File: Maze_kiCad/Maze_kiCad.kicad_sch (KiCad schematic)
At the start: 9 parts, among them U1 ESP32-S2-DevKitC-1, U2 TSSP58038, U3 TSSP58038, U4 TSSP58038, U5 TSSP58038, U6 TSSP58038, U7 TSSP58038, U8 GY-521

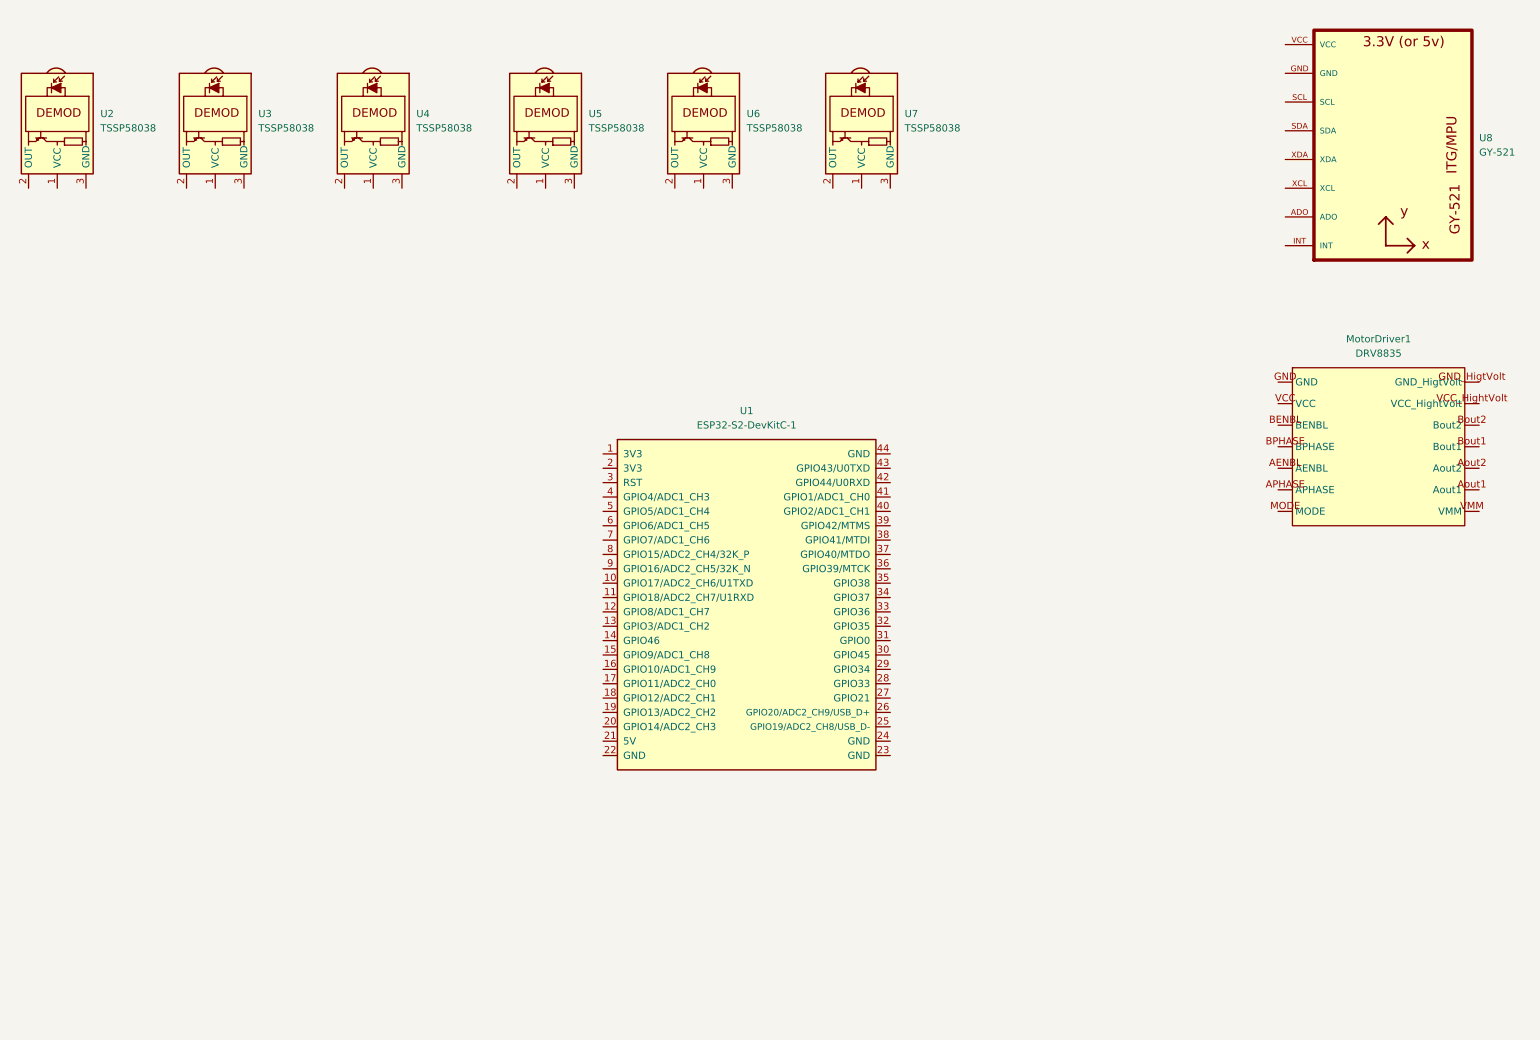
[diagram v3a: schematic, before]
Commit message: add ultra sonic symbol and footprint
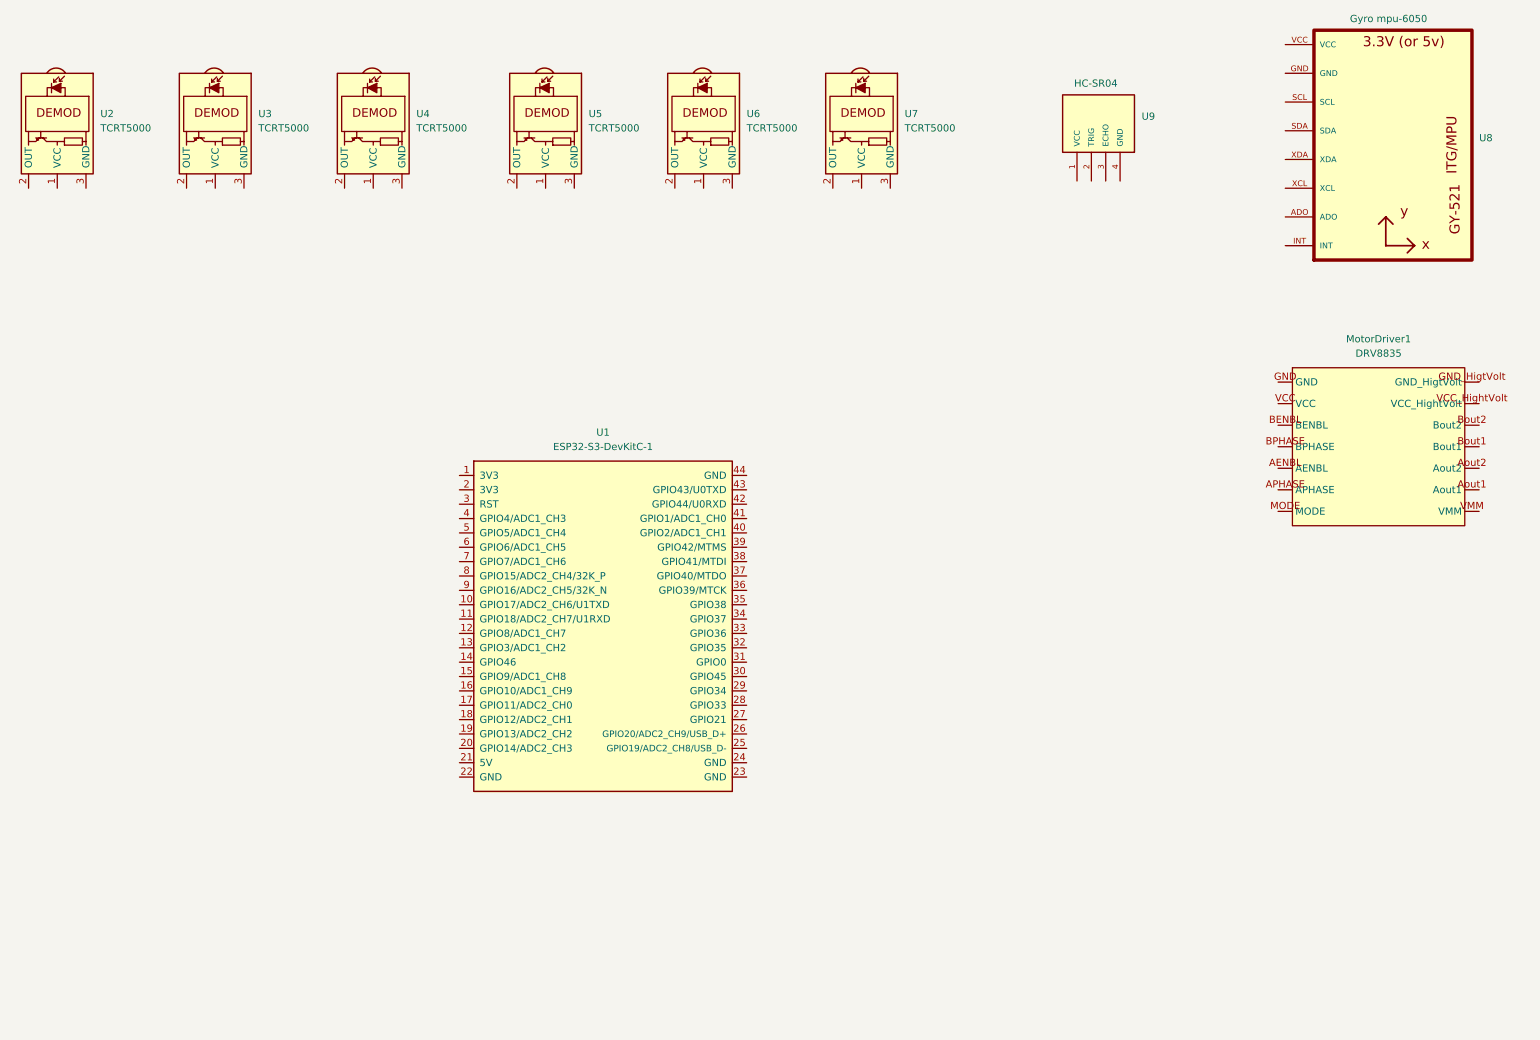
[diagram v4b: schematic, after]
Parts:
- added U9: HC-SR04, ultrasonic:XCVR_HC-SR04, symbol ultrasonic:HC-SR04
- U1: value ESP32-S2-DevKitC-1 -> ESP32-S3-DevKitC-1
- U2, U3, U4, U5, U6, U7: value TSSP58038 -> TCRT5000
- U8: value GY-521 -> Gyro mpu-6050
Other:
- moved on the sheet: U1
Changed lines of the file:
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@@
 			)
 		)
-		(property "Value" "TSSP58038"
+		(property "Value" "TCRT5000"
 			(at 144.78 35.0949 90)
 			(effects
@@
 			)
 		)
-		(property "Value" "TSSP58038"
+		(property "Value" "TCRT5000"
 			(at 116.84 35.0949 90)
 			(effects
@@
 			)
 		)
-		(property "Value" "TSSP58038"
+		(property "Value" "TCRT5000"
 			(at 30.48 35.0949 90)
 			(effects
@@
 			)
 		)
-		(property "Value" "TSSP58038"
+		(property "Value" "TCRT5000"
 			(at 58.42 35.0949 90)
 			(effects
@@
 			)
 		)
-		(property "Value" "TSSP58038"
+		(property "Value" "TCRT5000"
 			(at 172.72 35.0949 90)
 			(effects
@@
 	(symbol
 		(lib_id "PCM_Espressif:ESP32-S2-DevKitC-1")
-		(at 144.78 118.11 0)
+		(at 119.38 121.92 0)
 		(unit 1)
 		(exclude_from_sim no)
@@
 		(fields_autoplaced yes)
 		(property "Reference" "U1"
-			(at 144.78 85.09 0)
-			(effects
-				(font
-					(size 1.27 1.27)
-				)
-			)
-		)
-		(property "Value" "ESP32-S2-DevKitC-1"
-			(at 144.78 87.63 0)
+			(at 119.38 88.9 0)
+			(effects
+				(font
+					(size 1.27 1.27)
+				)
+			)
+		)
+		(property "Value" "ESP32-S3-DevKitC-1"
+			(at 119.38 91.44 0)
 			(effects
 				(font
@@
 		)
 		(property "Footprint" "PCM_Espressif:ESP32-S2-DevKitC-1"
-			(at 144.78 151.13 0)
+			(at 119.38 154.94 0)
 			(effects
 				(font
@@
 		)
 		(property "Datasheet" "https://docs.espressif.com/projects/esp-idf/en/latest/esp32s2/hw-reference/esp32s2/user-guide-s2-devkitc-1.html"
-			(at 156.21 153.67 0)
+			(at 130.81 157.48 0)
 			(effects
 				(font
@@
 		)
 		(property "Description" "ESP32-S2-DevKitC-1"
-			(at 144.78 118.11 0)
+			(at 119.38 121.92 0)
 			(effects
 				(font
@@
 		(on_board yes)
 		(dnp no)
-		(fields_autoplaced yes)
 		(property "Reference" "U8"
 			(at 274.32 36.8299 0)
@@
 			)
 		)
-		(property "Value" "GY-521"
-			(at 274.32 39.3699 0)
+		(property "Value" "Gyro mpu-6050"
+			(at 251.46 15.748 0)
 			(effects
 				(font
@@
 			)
 		)
-		(property "Value" "TSSP58038"
+		(property "Value" "TCRT5000"
 			(at 86.36 35.0949 90)
 			(effects
@@
 					(unit 1)
 				)
+			)
+		)
+	)
+	(symbol
+		(lib_id "ultrasonic:HC-SR04")
+		(at 205.74 39.37 90)
+		(unit 1)
+		(exclude_from_sim no)
+		(in_bom yes)
+		(on_board yes)
+		(dnp no)
+		(property "Reference" "U9"
+			(at 214.63 33.0199 90)
+			(effects
+				(font
+					(size 1.27 1.27)
+				)
+				(justify right)
+			)
+		)
+		(property "Value" "HC-SR04"
+			(at 202.692 27.178 90)
+			(effects
+				(font
+					(size 1.27 1.27)
+				)
+				(justify right)
+			)
+		)
+		(property "Footprint" "ultrasonic:XCVR_HC-SR04"
+			(at 205.74 39.37 0)
+			(effects
+				(font
+					(size 1.27 1.27)
+				)
+				(justify bottom)
+				(hide yes)
+			)
+		)
+		(property "Datasheet" ""
+			(at 205.74 39.37 0)
+			(effects
+				(font
+					(size 1.27 1.27)
+				)
+				(hide yes)
+			)
+		)
+		(property "Description" ""
+			(at 205.74 39.37 0)
+			(effects
+				(font
+					(size 1.27 1.27)
+				)
+				(hide yes)
+			)
+		)
+		(property "MF" "SparkFun Electronics"
+			(at 205.74 39.37 0)
+			(effects
+				(font
+					(size 1.27 1.27)
+				)
+				(justify bottom)
+				(hide yes)
+			)
+		)
+		(property "Description_1" "\nHC-SR04 Ultrasonic Sensor Qwiic Platform Evaluation Expansion Board\n"
+			(at 205.74 39.37 0)
+			(effects
+				(font
+					(size 1.27 1.27)
+				)
+				(justify bottom)
+				(hide yes)
+			)
+		)
+		(property "Package" "None"
+			(at 205.74 39.37 0)
+			(effects
+				(font
+					(size 1.27 1.27)
+				)
+				(justify bottom)
+				(hide yes)
+			)
+		)
+		(property "Price" "None"
+			(at 205.74 39.37 0)
+			(effects
+				(font
+					(size 1.27 1.27)
+				)
+				(justify bottom)
+				(hide yes)
+			)
+		)
+		(property "Check_prices" "https://www.snapeda.com/parts/HC-SR04/SparkFun+Electronics/view-part/?ref=eda"
+			(at 205.74 39.37 0)
+			(effects
+				(font
+					(size 1.27 1.27)
+				)
+				(justify bottom)
+				(hide yes)
+			)
+		)
+		(property "SnapEDA_Link" "https://www.snapeda.com/parts/HC-SR04/SparkFun+Electronics/view-part/?ref=snap"
+			(at 205.74 39.37 0)
+			(effects
+				(font
+					(size 1.27 1.27)
+				)
+				(justify bottom)
+				(hide yes)
+			)
+		)
+		(property "MP" "HC-SR04"
+			(at 205.74 39.37 0)
+			(effects
+				(font
+					(size 1.27 1.27)
+				)
+				(justify bottom)
+				(hide yes)
+			)
+		)
+		(property "Availability" "Not in stock"
+			(at 205.74 39.37 0)
+			(effects
+				(font
+					(size 1.27 1.27)
+				)
+				(justify bottom)
+				(hide yes)
+			)
+		)
+		(property "MANUFACTURER" "Osepp"
+			(at 205.74 39.37 0)
+			(effects
+				(font
+					(size 1.27 1.27)
+				)
+				(justify bottom)
+				(hide yes)
+			)
+		)
+		(pin "2"
+		)
+		(pin "3"
+		)
+		(pin "4"
+		)
+		(pin "1"
+		)
+		(instances
+			(project "Maze_kiCad"
+				(path "/22108416-3e7d-4108-b707-2b088264c2dd"
+					(reference "U9")
+					(unit 1)
+				)

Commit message: Create all power inputs flags (5v and 7.4volt).
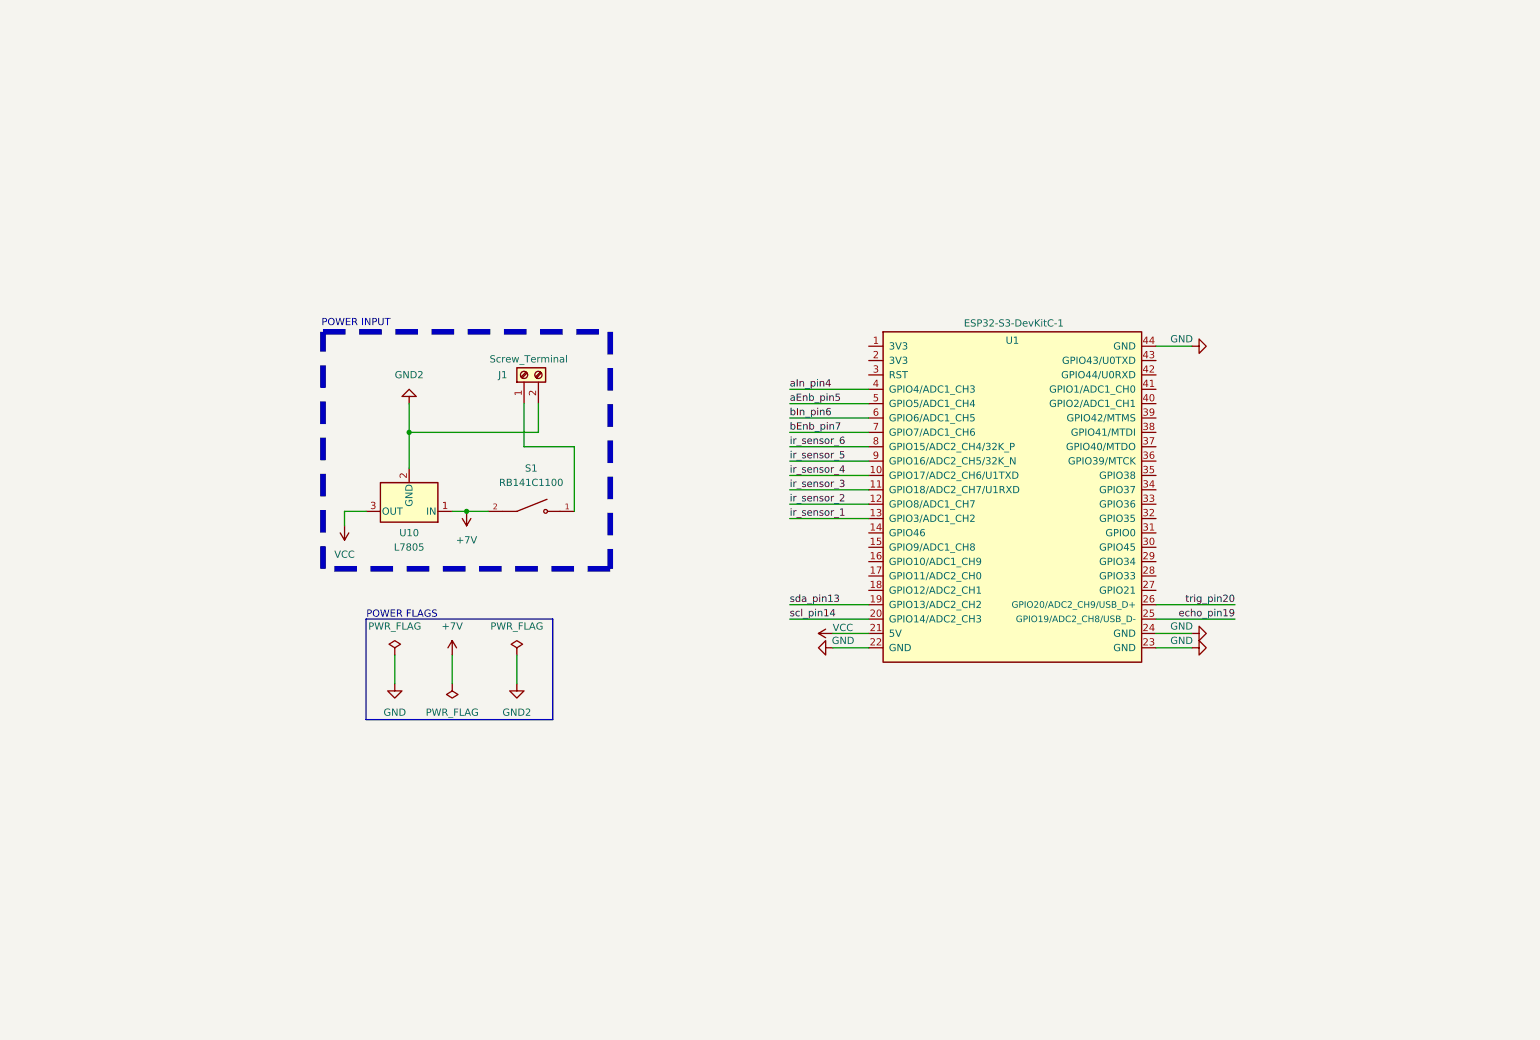
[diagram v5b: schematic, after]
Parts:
- removed MotorDriver1: DRV8835, drv8835:drv8835, symbol drv8835:DRV8835
- removed U2, U3, U4, U5, U6, U7: TCRT5000, OptoDevice:Vishay_MINICAST-3Pin, symbol Sensor_Proximity:TSSP58038
- removed U8: Gyro mpu-6050, mpu6050:GY-521, symbol mpu6050:GY-521
- removed U9: HC-SR04, ultrasonic:XCVR_HC-SR04, symbol ultrasonic:HC-SR04
- added J1: Screw_Terminal, TerminalBlock_Phoenix:TerminalBlock_Phoenix_MPT-0,5-2-2.54_1x02_P2.54mm_Horizontal, symbol Connector:Screw_Terminal_01x02
- added S1: RB141C1100, RB141C1100:SW_RB141C1100, symbol RB141C1100:RB141C1100
- added U10: L7805, Connector_PinSocket_2.54mm:PinSocket_1x03_P2.54mm_Vertical, symbol Regulator_Linear:L7805
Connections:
- net ir_sensor_4: now reaches U1.10 (GPIO17/ADC2_CH6/U1TXD)
- net ir_sensor_3: now reaches U1.11 (GPIO18/ADC2_CH7/U1RXD)
- net ir_sensor_2: now reaches U1.12 (GPIO8/ADC1_CH7)
- net ir_sensor_1: now reaches U1.13 (GPIO3/ADC1_CH2)
- net sda_pin13: now reaches U1.19 (GPIO13/ADC2_CH2)
- net scl_pin14: now reaches U1.20 (GPIO14/ADC2_CH3)
- net VCC: now reaches U1.21 (5V)
- net VCC: now also U10.3 (OUT)
- net GND: now reaches U1.22 (GND)
- net GND: now also U1.23 (GND), U1.24 (GND), U1.44 (GND)
- net echo_pin19: now reaches U1.25 (GPIO19/ADC2_CH8/USB_D-)
- net trig_pin20: now reaches U1.26 (GPIO20/ADC2_CH9/USB_D+)
- net aIn_pin4: now reaches U1.4 (GPIO4/ADC1_CH3)
- net aEnb_pin5: now reaches U1.5 (GPIO5/ADC1_CH4)
- net bIn_pin6: now reaches U1.6 (GPIO6/ADC1_CH5)
- net bEnb_pin7: now reaches U1.7 (GPIO7/ADC1_CH6)
- net ir_sensor_6: now reaches U1.8 (GPIO15/ADC2_CH4/32K_P)
- net ir_sensor_5: now reaches U1.9 (GPIO16/ADC2_CH5/32K_N)
- new net: J1.1 (Pin_1), S1.1
- new net +7V: S1.2, U10.1 (IN)
- new net GND2: J1.2 (Pin_2), U10.2 (GND)
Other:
- note added: "POWER FLAGS"
- note added: "POWER INPUT"
- moved on the sheet: U1

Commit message: Create all connections for 6 ir sensors and esp32-s3
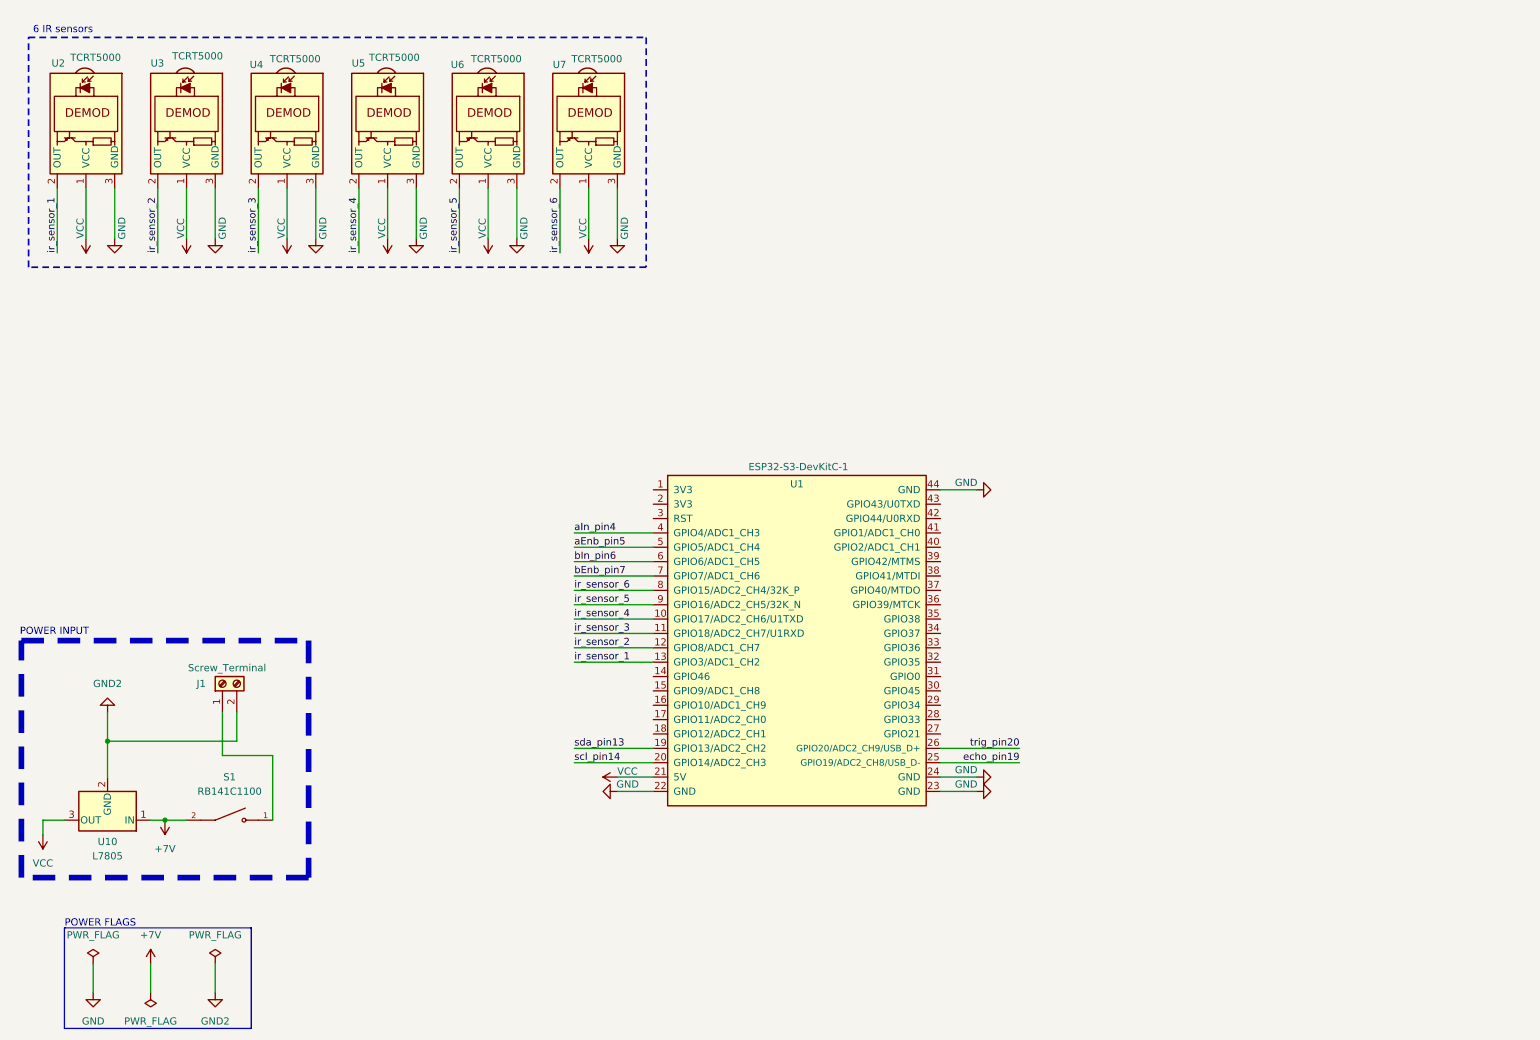
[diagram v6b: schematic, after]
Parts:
- added U2, U3, U4, U5, U6, U7: TCRT5000, OptoDevice:Vishay_MINICAST-3Pin, symbol Sensor_Proximity:TSSP58038
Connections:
- net GND: now also U2.3 (GND), U3.3 (GND), U4.3 (GND), U5.3 (GND), U6.3 (GND), U7.3 (GND)
- net VCC: now also U2.1 (VCC), U3.1 (VCC), U4.1 (VCC), U5.1 (VCC), U6.1 (VCC), U7.1 (VCC)
- net ir_sensor_1: now also U2.2 (OUT)
- net ir_sensor_2: now also U3.2 (OUT)
- net ir_sensor_3: now also U4.2 (OUT)
- net ir_sensor_4: now also U5.2 (OUT)
- net ir_sensor_5: now also U6.2 (OUT)
- net ir_sensor_6: now also U7.2 (OUT)
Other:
- note added: "6 IR sensors"
- moved on the sheet: J1, S1, U1, U10
